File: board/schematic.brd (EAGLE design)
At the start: 81.3 x 97.8 mm, 53 parts, among them J2 AVR_SPI_PROG_3X2PTH, U1 328P, U2 SN74HC595N, U3 SN74HC595N, U4 SN74HC595N, U5 SN74HC595N

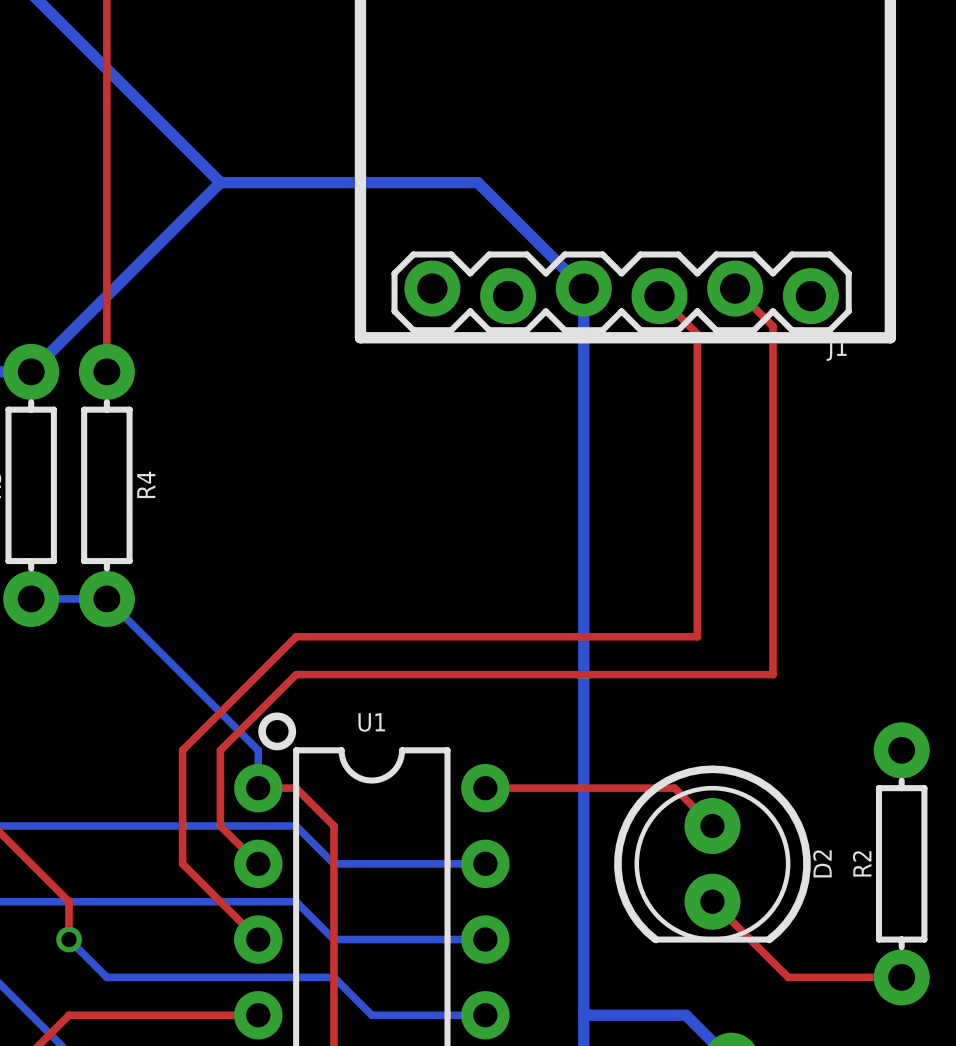
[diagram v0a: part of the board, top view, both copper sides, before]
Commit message: Fix crossed rx/tx
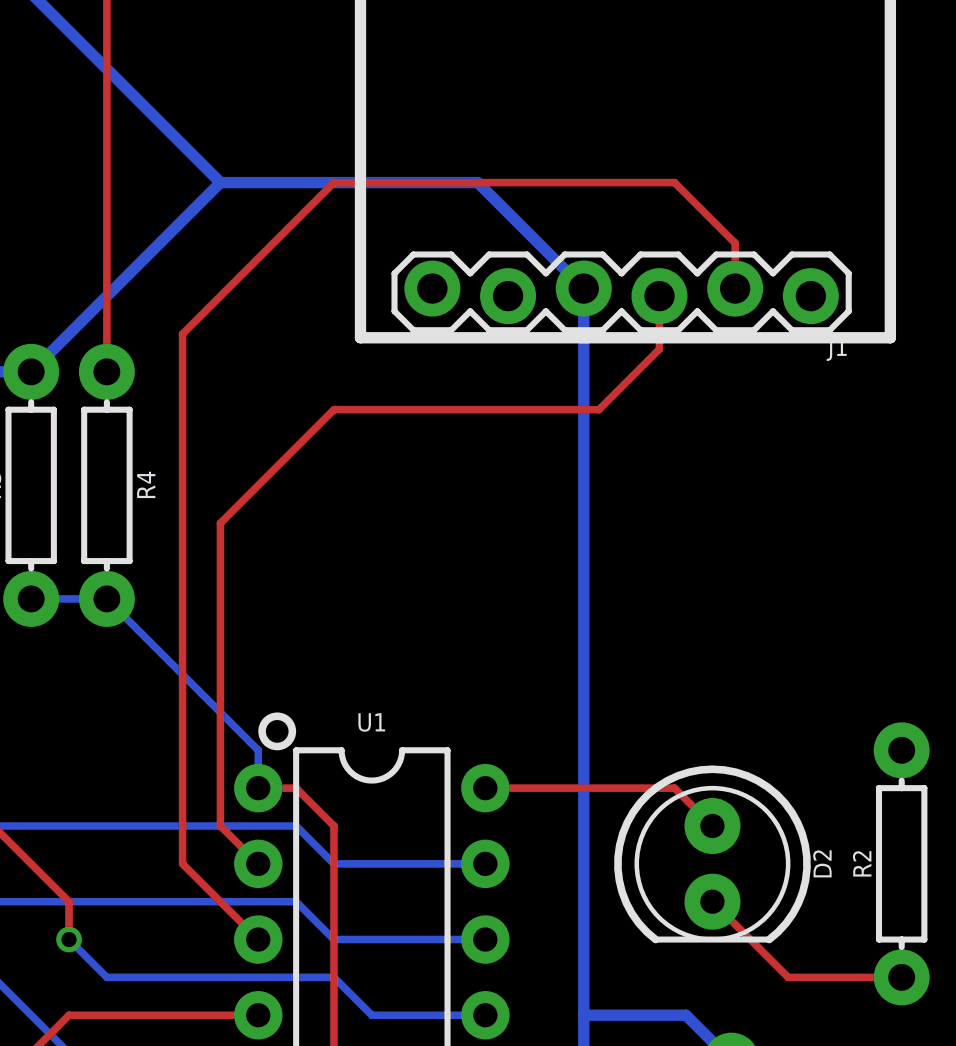
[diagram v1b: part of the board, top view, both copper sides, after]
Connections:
- net RXD: now also J1.3; no longer J1.2
- net TXD: now also J1.2; no longer J1.3
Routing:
- net RXD: track 37.4 -> 30.9 mm
- net TXD: track 38.2 -> 44.4 mm
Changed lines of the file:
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@@
 <signal name="RXD">
 <contactref element="U1" pad="2"/>
-<contactref element="J1" pad="2"/>
-<wire x1="149.86" y1="49.53" x2="147.32" y2="46.99" width="0.254" layer="1"/>
-<wire x1="147.32" y1="46.99" x2="147.32" y2="44.45" width="0.254" layer="1"/>
 <wire x1="148.59" y1="43.18" x2="147.32" y2="44.45" width="0.254" layer="1"/>
-<wire x1="149.86" y1="49.53" x2="165.862" y2="49.53" width="0.254" layer="1"/>
-<wire x1="165.862" y1="61.214" x2="165.862" y2="49.53" width="0.254" layer="1"/>
-<wire x1="165.862" y1="61.214" x2="164.592" y2="62.484" width="0.254" layer="1"/>
+<contactref element="J1" pad="3"/>
+<wire x1="147.32" y1="54.61" x2="151.13" y2="58.42" width="0.254" layer="1"/>
+<wire x1="151.13" y1="58.42" x2="160.02" y2="58.42" width="0.254" layer="1"/>
+<wire x1="160.02" y1="58.42" x2="162.052" y2="60.452" width="0.254" layer="1"/>
+<wire x1="162.052" y1="60.452" x2="162.052" y2="62.23" width="0.254" layer="1"/>
+<wire x1="147.32" y1="44.45" x2="147.32" y2="54.61" width="0.254" layer="1"/>
 </signal>
 <signal name="TXD">
 <contactref element="U1" pad="3"/>
-<contactref element="J1" pad="3"/>
 <wire x1="148.59" y1="40.64" x2="146.05" y2="43.18" width="0.254" layer="1"/>
-<wire x1="146.05" y1="43.18" x2="146.05" y2="46.99" width="0.254" layer="1"/>
-<wire x1="146.05" y1="46.99" x2="149.86" y2="50.8" width="0.254" layer="1"/>
-<wire x1="149.86" y1="50.8" x2="163.322" y2="50.8" width="0.254" layer="1"/>
-<wire x1="163.322" y1="60.96" x2="163.322" y2="50.8" width="0.254" layer="1"/>
-<wire x1="163.322" y1="60.96" x2="162.052" y2="62.23" width="0.254" layer="1"/>
+<contactref element="J1" pad="2"/>
+<wire x1="146.05" y1="43.18" x2="146.05" y2="60.96" width="0.254" layer="1"/>
+<wire x1="146.05" y1="60.96" x2="151.13" y2="66.04" width="0.254" layer="1"/>
+<wire x1="151.13" y1="66.04" x2="162.56" y2="66.04" width="0.254" layer="1"/>
+<wire x1="162.56" y1="66.04" x2="164.592" y2="64.008" width="0.254" layer="1"/>
+<wire x1="164.592" y1="64.008" x2="164.592" y2="62.484" width="0.254" layer="1"/>
 </signal>
 <signal name="SCK">
